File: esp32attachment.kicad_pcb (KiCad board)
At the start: 2 copper layers, 157.6 x 60 mm, 36 parts, among them J1 B2B-PH-SM4-TB, J2 B2B-PH-SM4-TB, J3 B2B-PH-SM4-TB, J4 B2B-PH-SM4-TB, J5 B2B-PH-SM4-TB, J6 B2B-PH-SM4-TB, J7 BATTERY_CONNECTOR, Q1 AOD4184A, Q2 AOD4184A, Q3 AOD4184A, Q4 AOD4184A, Q5 AOD4184A, Q6 AOD4184A, U1 ESP32-DEVKIT-V1, U2 PC847, U3 PC827

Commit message: wilkkur review1 changes; still missing mounting holes
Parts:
- added G***: LOGO, symbols:usagi, F.Cu at (145.9, 87.6)
- added G***: LOGO, symbols:soyo, F.Cu at (149.9, 59.2)
- moved R7 36.3 mm to (83.0, 94.9)
- moved R9 36.3 mm to (83.0, 58.6)
- moved R1 24.6 mm to (107.2, 98.1), turned to 180 degrees
- moved U2 20.6 mm to (103.3, 97.8), turned to 180 degrees
- moved R4 17.4 mm to (107.2, 83.2), turned to 180 degrees
- moved R2 17.0 mm to (107.2, 93.0), turned to 180 degrees
- moved R3 14.1 mm to (107.2, 88.0), turned to 180 degrees
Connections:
- R1 pad 1: /GPIO12 -> /GPIO25
- R2 pad 1: /GPIO13 -> /GPIO14
- R3 pad 1: /GPIO14 -> /GPIO12
- R4 pad 1: /GPIO25 -> /GPIO13
- R7 pad 1: /FET_GATE1 -> /FET_GATE3
- R9 pad 1: /FET_GATE3 -> /FET_GATE1
- U2 pad 11: /FET_GATE3 -> /FET_GATE1
- U2 pad 15: /FET_GATE1 -> /FET_GATE3
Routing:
- net GND: track 186.8 -> 9.91 mm, vias 8 -> 4
- net GNDPWR: track 78.3 -> 40.3 mm, vias 18 -> 23
- net /GPIO12: track 68.7 -> 39.0 mm, vias 2 -> 0
- net /GPIO13: track 67.0 -> 38.0 mm, vias 2 -> 0
- net /GPIO14: track 60.9 -> 39.6 mm, vias 2 -> 0
- net /FET_GATE3: track 41.3 -> 21.5 mm, vias 2 -> 0
- net /GPIO25: track 56.7 -> 38.5 mm, vias 2 -> 0
- net +12V: track 515.7 -> 498.4 mm
- net /FET_GATE1: track 56.0 -> 38.8 mm, vias 2 -> 0
- net /FET_GATE4: track 89.4 -> 101.3 mm, vias 2 -> 0
- net /FET_GATE2: track 38.9 -> 27.1 mm, vias 2 -> 0
- net Net-(R2-Pad2): track 3.62 -> 3.06 mm
- added copper zone on F.Cu, net GNDPWR
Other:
- board size 157.6 x 60 mm -> 156.2 x 57.2 mm
- board text added: "なんで『春日影』 やったの!？"

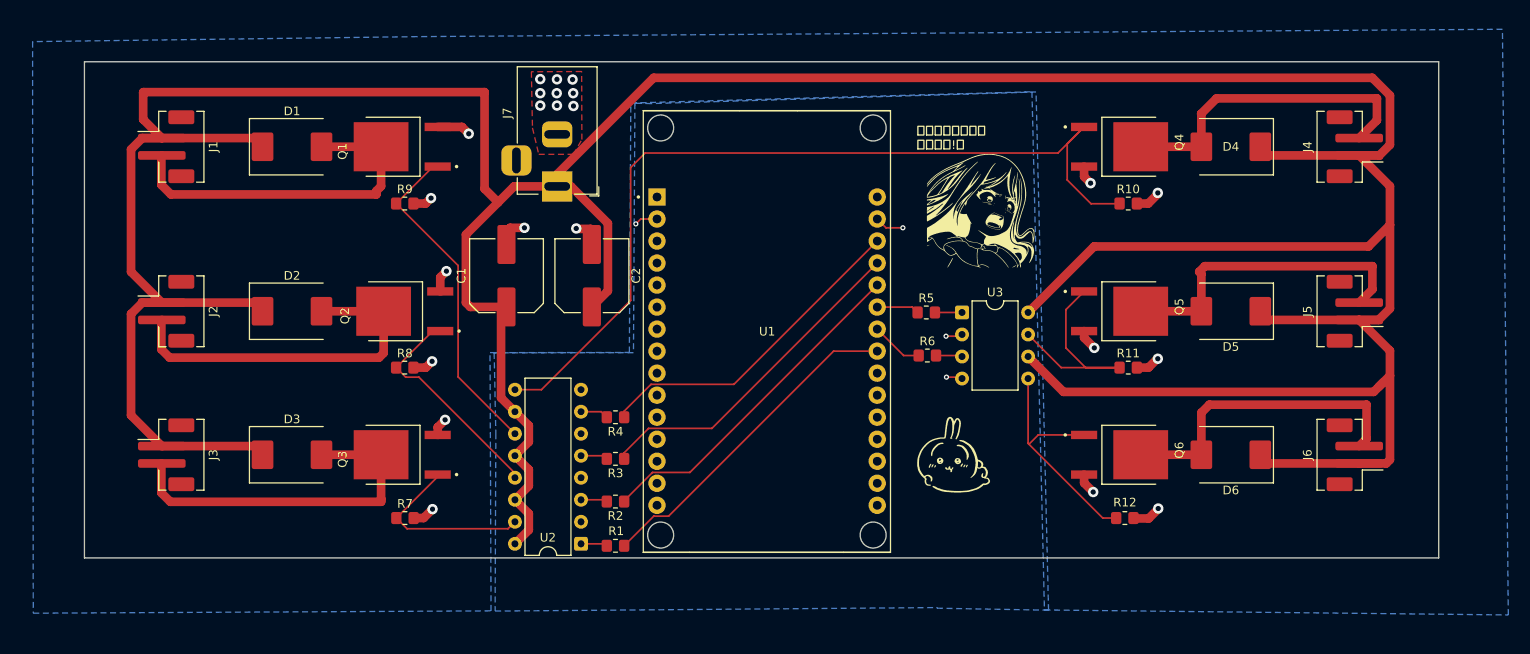
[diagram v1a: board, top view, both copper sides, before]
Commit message: fixed some gnd issues;added sakiko on back :drool:
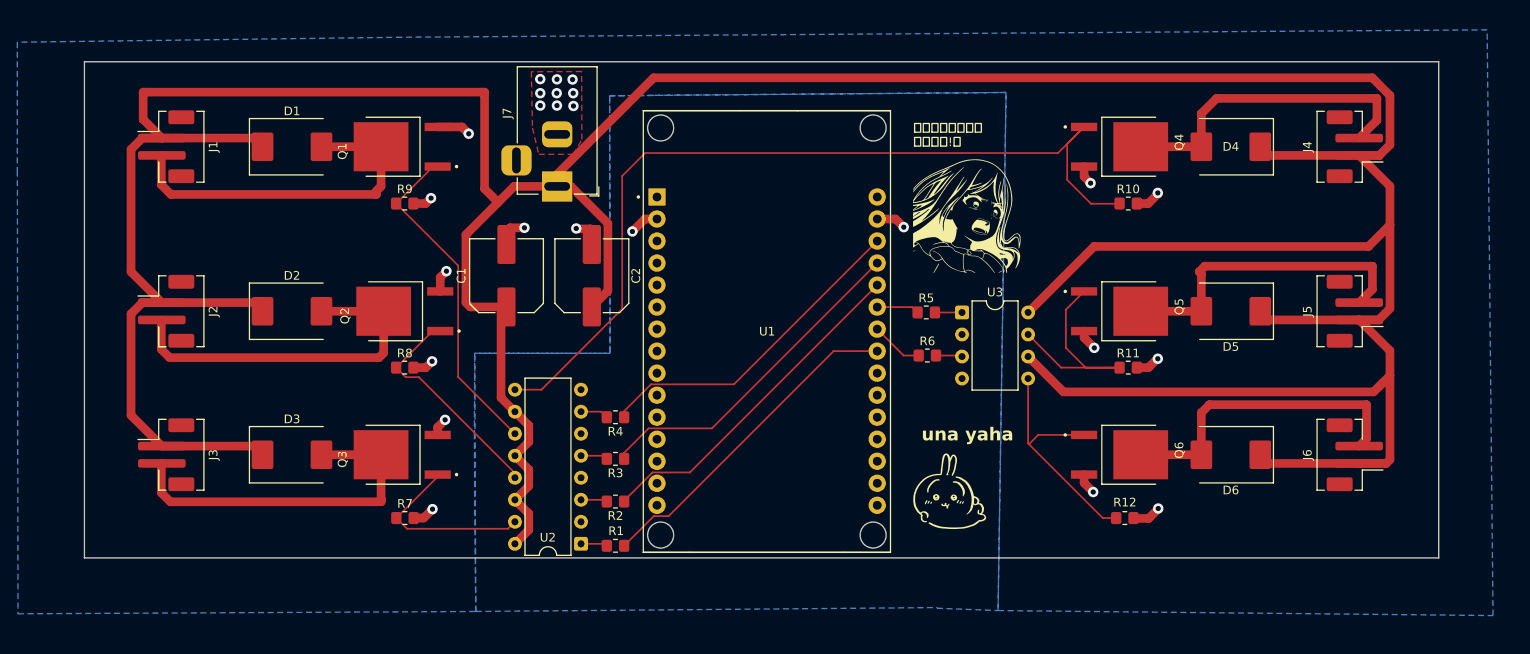
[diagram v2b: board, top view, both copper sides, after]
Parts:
- added G***: LOGO, symbols:sakirevised, B.Cu at (69.9, 65.4)
- moved G*** 4.23 mm to (145.5, 91.8)
- moved G*** 1.72 mm to (148.3, 59.9)
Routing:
- net GND: track 9.91 -> 7.39 mm, vias 4 -> 2
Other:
- board text added: "una yaha"

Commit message: added M2.5 mounting holes
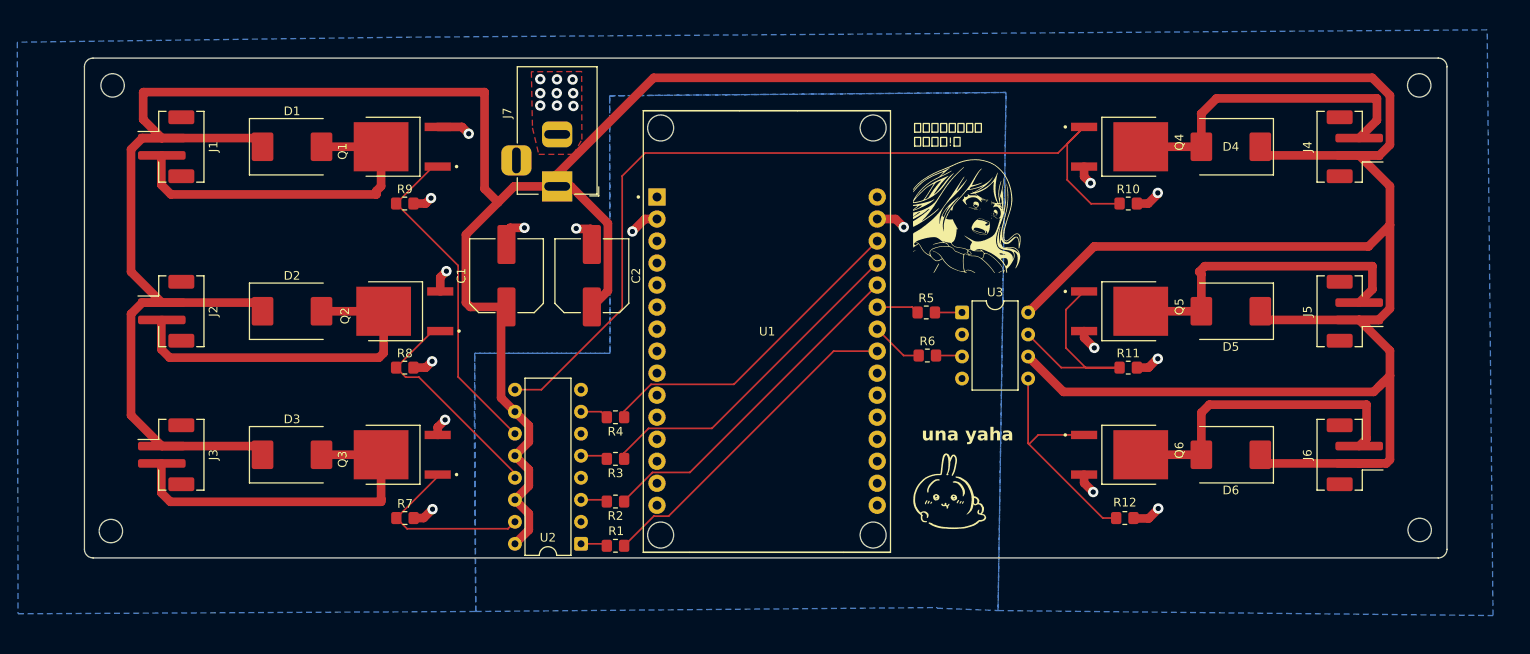
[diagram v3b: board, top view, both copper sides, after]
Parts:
- added REF**: MountingHole_2.7mm_M2.5, MountingHole:MountingHole_2.7mm_M2.5, F.Cu at (199.9, 45.0)
- added REF**: MountingHole_2.7mm_M2.5, MountingHole:MountingHole_2.7mm_M2.5, F.Cu at (49.0, 96.4)
- added REF**: MountingHole_2.7mm_M2.5, MountingHole:MountingHole_2.7mm_M2.5, F.Cu at (200.0, 96.2)
- added REF**: MountingHole_2.7mm_M2.5, MountingHole:MountingHole_2.7mm_M2.5, F.Cu at (49.2, 45.0)
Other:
- board size 156.2 x 57.2 mm -> 157.2 x 57.6 mm

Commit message: aligned mounting holes and fixed filled zones
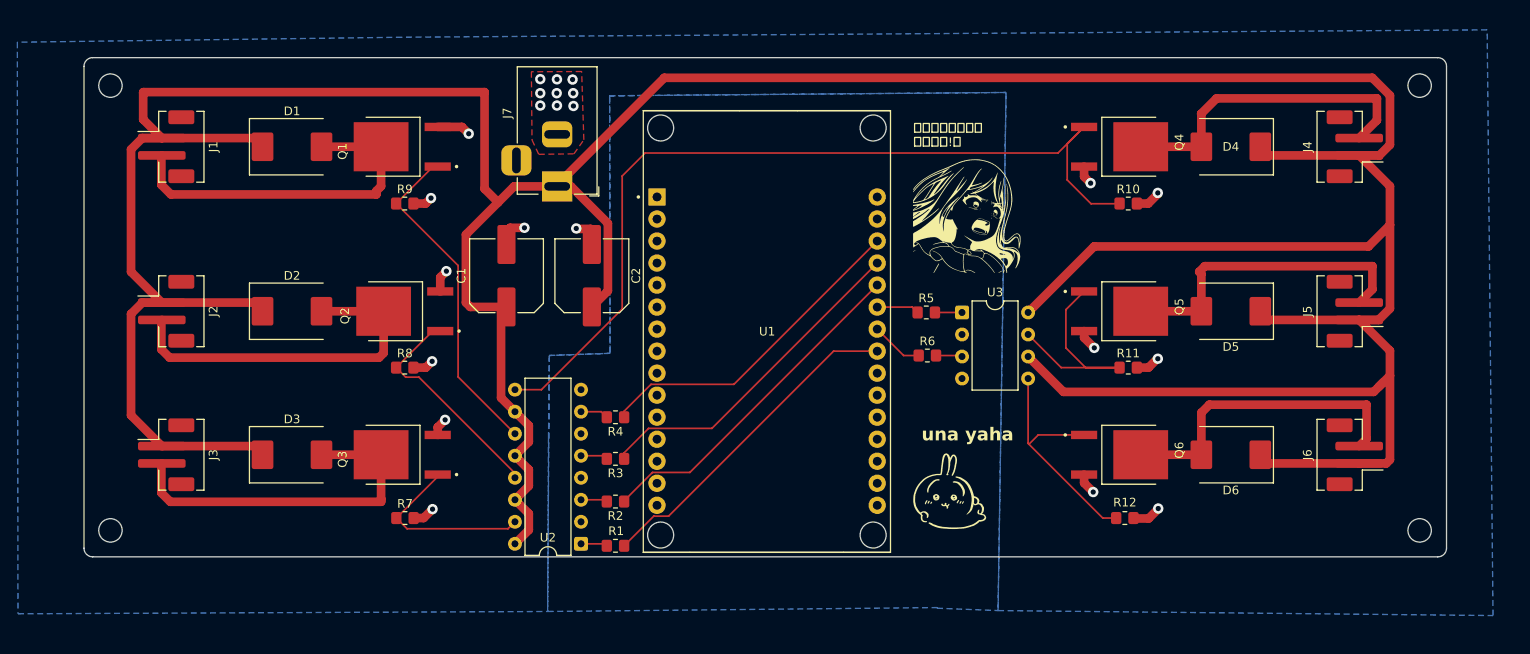
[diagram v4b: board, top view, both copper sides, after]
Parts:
- moved REF** 0.25 mm to (49.0, 45.0)
- moved REF** 0.09 mm to (49.0, 96.3)
- moved REF** 0.06 mm to (200.0, 45.0)
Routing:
- net GND: track 7.39 -> 0.50 mm, vias 2 -> 0
- net +12V: track 498.4 -> 497.7 mm
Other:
- board size 157.2 x 57.6 mm -> 157.1 x 57.6 mm
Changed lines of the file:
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@@
 	(footprint "MountingHole:MountingHole_2.7mm_M2.5"
 		(layer "F.Cu")
-		(at 199.95 44.975)
+		(at 200 45)
 		(descr "Mounting Hole 2.7mm, M2.5, no annular, generated by kicad-footprint-generator mountinghole.py")
 		(tags "mountinghole M2.5")
@@
 	(footprint "MountingHole:MountingHole_2.7mm_M2.5"
 		(layer "F.Cu")
-		(at 49.05 96.375)
+		(at 49 96.3)
 		(descr "Mounting Hole 2.7mm, M2.5, no annular, generated by kicad-footprint-generator mountinghole.py")
 		(tags "mountinghole M2.5")
@@
 	(footprint "MountingHole:MountingHole_2.7mm_M2.5"
 		(layer "F.Cu")
-		(at 200 96.25)
+		(at 200 96.3)
 		(descr "Mounting Hole 2.7mm, M2.5, no annular, generated by kicad-footprint-generator mountinghole.py")
 		(tags "mountinghole M2.5")
@@
 	(footprint "MountingHole:MountingHole_2.7mm_M2.5"
 		(layer "F.Cu")
-		(at 49.25 44.975)
+		(at 49 45)
 		(descr "Mounting Hole 2.7mm, M2.5, no annular, generated by kicad-footprint-generator mountinghole.py")
 		(tags "mountinghole M2.5")
@@
 		(embedded_fonts no)
 	)
-	(gr_arc
-		(start 203.15 98.475)
-		(mid 202.857107 99.182107)
-		(end 202.15 99.475)
+	(gr_line
+		(start 203.1 42.8)
+		(end 203.1 98.35)
 		(stroke
 			(width 0.05)
-			(type default)
+			(type solid)
 		)
 		(layer "Edge.Cuts")
 	)
-	(gr_line
-		(start 203.15 42.825)
-		(end 203.15 98.475)
+	(gr_arc
+		(start 46.95 99.35)
+		(mid 46.242893 99.057107)
+		(end 45.95 98.35)
 		(stroke
 			(width 0.05)
@@
 		(layer "Edge.Cuts")
 	)
-	(gr_arc
-		(start 46 42.825)
-		(mid 46.292893 42.117893)
-		(end 47 41.825)
+	(gr_line
+		(start 202.1 99.35)
+		(end 46.95 99.35)
 		(stroke
 			(width 0.05)
-			(type default)
+			(type solid)
 		)
 		(layer "Edge.Cuts")
 	)
 	(gr_arc
-		(start 202.15 41.825)
-		(mid 202.857107 42.117893)
-		(end 203.15 42.825)
+		(start 203.1 98.35)
+		(mid 202.807107 99.057107)
+		(end 202.1 99.35)
 		(stroke
 			(width 0.05)
@@
 		(layer "Edge.Cuts")
 	)
-	(gr_line
-		(start 202.15 99.475)
-		(end 47 99.475)
+	(gr_arc
+		(start 45.95 42.775)
+		(mid 46.242893 42.067893)
+		(end 46.95 41.775)
 		(stroke
 			(width 0.05)
@@
 	)
 	(gr_arc
-		(start 47 99.475)
-		(mid 46.292893 99.182107)
-		(end 46 98.475)
+		(start 202.1 41.774688)
+		(mid 202.816112 42.076567)
+		(end 203.1 42.8)
 		(stroke
 			(width 0.05)
@@
 	)
 	(gr_line
-		(start 46 98.475)
-		(end 46 42.825)
+		(start 45.95 98.35)
+		(end 45.95 42.775)
 		(stroke
 			(width 0.05)
-			(type default)
+			(type solid)
 		)
 		(layer "Edge.Cuts")
 	)
 	(gr_line
-		(start 47 41.825)
-		(end 202.15 41.825)
+		(start 46.95 41.775)
+		(end 202.1 41.775)
 		(stroke
 			(width 0.05)
@@
 	)
 	(segment
+		(start 196.576 46.136108)
+		(end 196.576 51.824)
+		(width 1)
+		(layer "F.Cu")
+		(net 1)
+	)
+	(segment
 		(start 54.925 51.05)
 		(end 52.681734 51.05)
@@
 	)
 	(segment
-		(start 194.539892 44.1)
-		(end 196.576 46.136108)
-		(width 1)
-		(layer "F.Cu")
-		(net 1)
-	)
-	(segment
 		(start 182.625 53.05)
 		(end 193.025 53.05)
@@
 	)
 	(segment
-		(start 196.576 51.824)
-		(end 195.35 53.05)
-		(width 1)
-		(layer "F.Cu")
-		(net 1)
-	)
-	(segment
-		(start 100.525 56.625)
-		(end 100.525 55.225)
-		(width 1)
-		(layer "F.Cu")
-		(net 1)
-	)
-	(segment
 		(start 52.681734 70.025)
 		(end 51.374 71.332734)
@@
 	)
 	(segment
+		(start 100.525 56.625)
+		(end 100.525 56.45)
+		(width 1)
+		(layer "F.Cu")
+		(net 1)
+	)
+	(segment
 		(start 97.256 96.249)
 		(end 95.655 97.85)
@@
 	)
 	(segment
+		(start 195.35 53.05)
+		(end 193.025 53.05)
+		(width 1)
+		(layer "F.Cu")
+		(net 1)
+	)
+	(segment
 		(start 97.256 86.089)
 		(end 95.655 87.69)
@@
 	)
 	(segment
+		(start 196.576 51.824)
+		(end 195.35 53.05)
+		(width 1)
+		(layer "F.Cu")
+		(net 1)
+	)
+	(segment
 		(start 90.5 70.525)
 		(end 94.675 70.525)
@@
 	)
 	(segment
-		(start 196.576 46.136108)
-		(end 196.576 51.824)
-		(width 1)
-		(layer "F.Cu")
-		(net 1)
-	)
-	(segment
 		(start 94.675 70.525)
 		(end 94.054 71.146)
@@
 	)
 	(segment
-		(start 195.35 53.05)
-		(end 193.025 53.05)
+		(start 194.539892 44.1)
+		(end 196.576 46.136108)
 		(width 1)
 		(layer "F.Cu")
@@
 	)
 	(segment
+		(start 100.525 56.45)
+		(end 112.875 44.1)
+		(width 1)
+		(layer "F.Cu")
+		(net 1)
+	)
+	(segment
 		(start 196.576 75.576)
 		(end 196.576 78.45)
@@
 	)
 	(segment
-		(start 92.15 45.75)
-		(end 52.8 45.75)
+		(start 112.875 44.1)
+		(end 194.539892 44.1)
 		(width 1)
 		(layer "F.Cu")
@@
 	)
 	(segment
-		(start 193.025 53.05)
-		(end 196.576 56.601)
+		(start 92.15 45.75)
+		(end 52.8 45.75)
 		(width 1)
 		(layer "F.Cu")
@@
 	)
 	(segment
-		(start 100.525 55.225)
-		(end 111.65 44.1)
+		(start 193.025 53.05)
+		(end 196.576 56.601)
 		(width 1)
 		(layer "F.Cu")
@@
 	)
 	(segment
-		(start 111.65 44.1)
-		(end 194.539892 44.1)
-		(width 1)
-		(layer "F.Cu")
-		(net 1)
-	)
-	(segment
 		(start 54.925 51.05)
 		(end 65.542 51.05)
@@
 	)
 	(segment
-		(start 137.439 60.385)
-		(end 139.56 60.385)
-		(width 1)
-		(layer "F.Cu")
-		(net 35)
-	)
-	(segment
 		(start 147.22 73.705)
 		(end 147.025 73.9)
@@
 	)
 	(segment
-		(start 110.64 60.385)
-		(end 112.039 60.385)
-		(width 1)
-		(layer "F.Cu")
-		(net 35)
-	)
-	(segment
-		(start 109.2 61.825)
-		(end 110.64 60.385)
-		(width 1)
-		(layer "F.Cu")
-		(net 35)
-	)
-	(segment
-		(start 139.56 60.385)
-		(end 140.5 61.325)
-		(width 1)
-		(layer "F.Cu")
-		(net 35)
-	)
-	(segment
 		(start 147.22 78.785)
 		(end 147.06 78.625)
@@
 		(net 35)
 	)
-	(via
-		(at 109.2 61.825)
-		(size 1.2)
-		(drill 0.6)
-		(layers "F.Cu" "B.Cu")
-		(net 35)
-	)
-	(via
-		(at 140.5 61.325)
-		(size 1.2)
-		(drill 0.6)
-		(layers "F.Cu" "B.Cu")
-		(net 35)
-	)
 	(zone
 		(net 2)
@@
 			(clearance 0.4)
 		)
-		(min_thickness 0.25)
+		(min_thickness 0.17)
 		(filled_areas_thickness no)
 		(fill yes
@@
 		(polygon
 			(pts
-				(xy 97.55 43.4) (xy 97.675 49.875) (xy 98.4 52.925) (xy 102.4 52.925) (xy 103.375 51.225) (xy 103.35 43.375)
+				(xy 97.55 43.4) (xy 97.625 51.275) (xy 98.4 52.925) (xy 102.458007 52.869411) (xy 103.6 51.25) (xy 103.35 43.375)
 				(xy 97.6 43.4)
 			)
@@
 		(hatch edge 0.5)
 		(connect_pads
-			(clearance 0.4)
+			(clearance 0.3)
 		)
 		(min_thickness 0.2)
@@
 		(polygon
 			(pts
-				(xy 106.575 46.175) (xy 106.625 75.875) (xy 91.019209 75.865828) (xy 90.975 85.1) (xy 91.131483 105.65213)
+				(xy 106.575 46.175) (xy 106.625 75.875) (xy 99.625 76.125) (xy 99.525 85.575) (xy 99.425 105.65213)
 				(xy 144.35 105.2) (xy 144.325 105.275) (xy 151.375 105.547186) (xy 152.296526 45.790044) (xy 111.55 46.125)
 			)
@@
 		(priority 1)
 		(connect_pads
-			(clearance 0.5)
+			(clearance 0.3)
 		)
 		(min_thickness 0.25)
@@
 		(polygon
 			(pts
-				(xy 38.261734 54.794647) (xy 38.336734 105.919647) (xy 91.131483 105.65213) (xy 91.019209 75.865828)
-				(xy 106.625 75.875) (xy 106.575 46.175) (xy 152.296526 45.790044) (xy 151.375 105.547186) (xy 208.462902 106.122186)
+				(xy 38.261734 54.794647) (xy 38.336734 105.919647) (xy 99.425 105.65213) (xy 99.625 76.125) (xy 106.625 75.875)
+				(xy 106.575 46.175) (xy 152.296526 45.790044) (xy 151.375 105.547186) (xy 208.462902 106.122186)
 				(xy 207.786734 38.569647) (xy 82.611734 39.419647) (xy 38.261734 39.994647)
 			)

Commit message: swapped out jst but need to swap it again to screw term
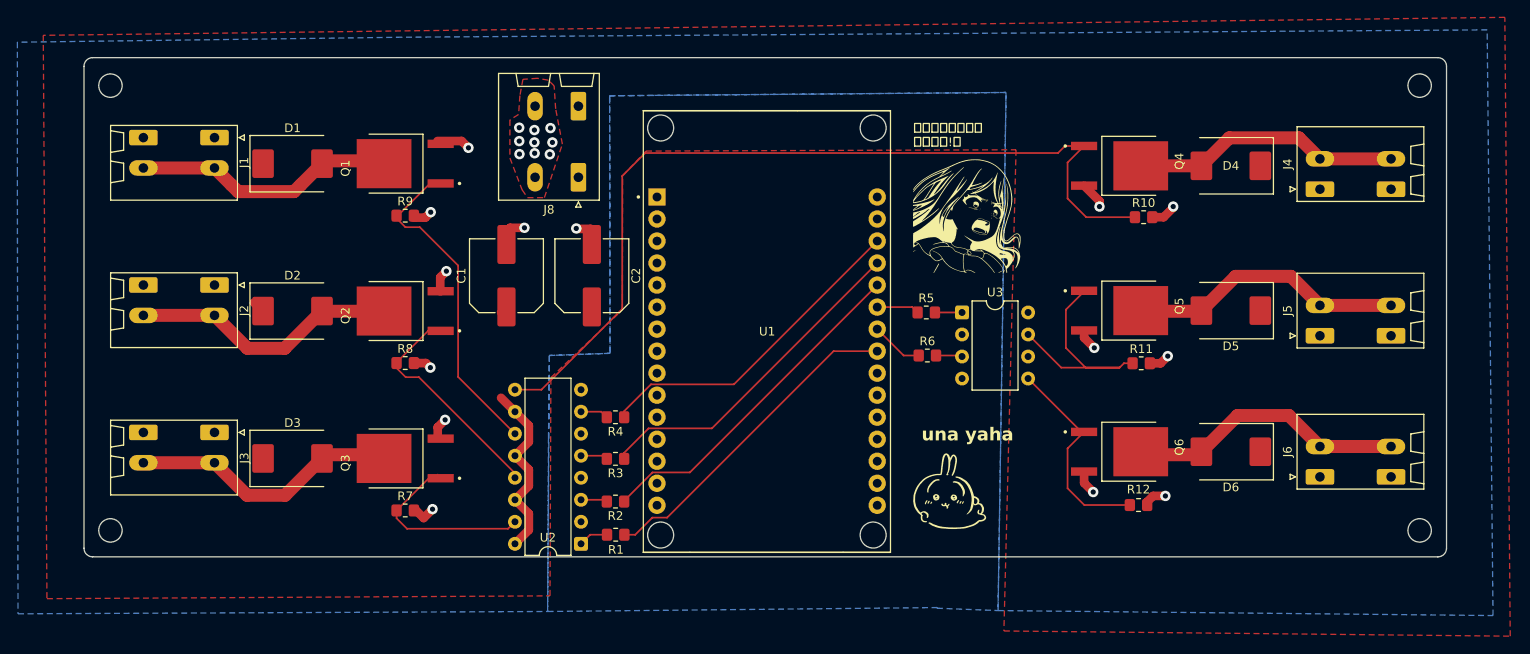
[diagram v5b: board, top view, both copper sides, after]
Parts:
- removed the G*** at (69.9, 65.4)
- removed J7: BATTERY_CONNECTOR, Connector_BarrelJack:BarrelJack_Horizontal
- added J8: Conn_01x02, Connector_Phoenix_SPT:PhoenixContact_SPT_2.5_2-H-5.0_1x02_P5.0mm_Horizontal, F.Cu at (103.0, 55.6)
- J1, J2, J3, J4, J5, J6: value B2B-PH-SM4-TB -> Conn_01x02; footprint Connector_JST:JST_PH_B2B-PH-SM4-TB_1x02-1MP_P2.00mm_Vertical -> Connector_Phoenix_SPT:PhoenixContact_SPT_1.5_2-H-3.5_1x02_P3.5mm_Horizontal
- moved J2 6.34 mm to (61.0, 68.0)
- moved J4 6.34 mm to (188.5, 57.0)
- moved J3 6.14 mm to (61.0, 85.0)
- moved J1 5.67 mm to (61.0, 51.0)
- moved J5 4.92 mm to (188.5, 73.8)
- moved J6 4.76 mm to (188.5, 90.1)
- moved R10 2.37 mm to (168.2, 60.2)
- moved D4 2.20 mm to (178.2, 54.2)
- moved Q4 2.20 mm to (165.4, 54.2)
- moved R12 2.17 mm to (167.6, 93.4)
- moved Q1 1.98 mm to (83.0, 54.0)
- moved D1 1.95 mm to (70.0, 54.0)
- moved R11 1.58 mm to (167.9, 77.0)
- moved R9 1.40 mm to (83.0, 60.0)
- moved R1 1.28 mm to (107.3, 96.8)
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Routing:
- net +12V: track 497.7 -> 24.7 mm
- net /FET_DRAIN1: track 41.3 -> 29.9 mm
- net /FET_DRAIN3: track 41.5 -> 30.8 mm
- net /FET_DRAIN2: track 41.7 -> 31.1 mm
- net /FET_DRAIN4: track 37.4 -> 31.2 mm
- net /FET_DRAIN5: track 36.7 -> 31.9 mm
- net /FET_DRAIN6: track 36.4 -> 32.1 mm
- net /FET_GATE6: track 28.5 -> 24.3 mm
- net /FET_GATE5: track 26.8 -> 28.4 mm
- net GNDPWR: track 40.3 -> 39.4 mm
- net /FET_GATE3: track 21.5 -> 22.3 mm
- net Net-(R1-Pad2): track 3.07 -> 3.75 mm
- net /FET_GATE1: track 38.8 -> 38.1 mm
- net /GPIO25: track 38.5 -> 37.9 mm
- net /FET_GATE2: track 27.1 -> 27.7 mm
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- added copper zone on F.Cu, net +12V
